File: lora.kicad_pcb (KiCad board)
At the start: 4 copper layers, 80.5 x 45 mm, 62 parts, among them J1 Conn_01x02, J11 Conn_Coaxial, J2 Humidity, J3 Temp, J4 Programming_Jumper, J5 Temp, J6 VDD, J7 GPS, J8 SIM800, J9 I2C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

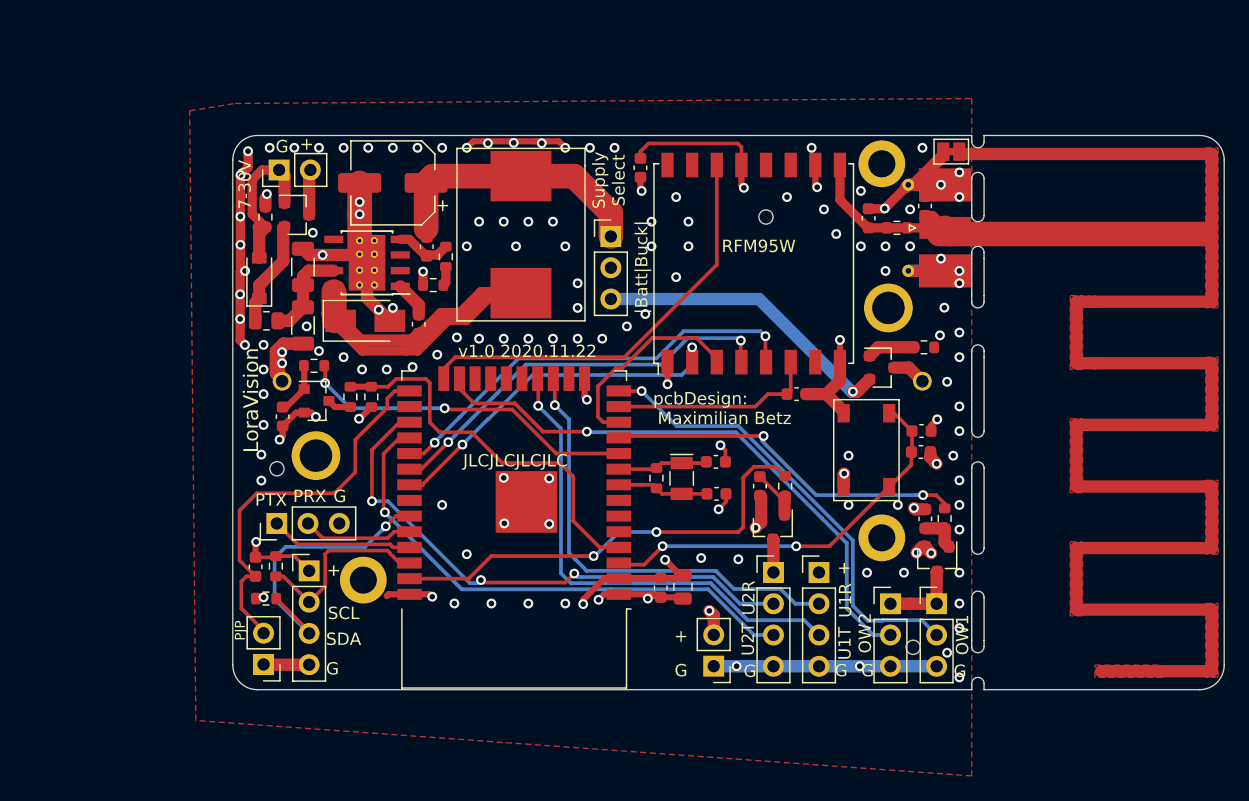
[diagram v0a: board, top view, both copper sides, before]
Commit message: updated pcb from schematic.
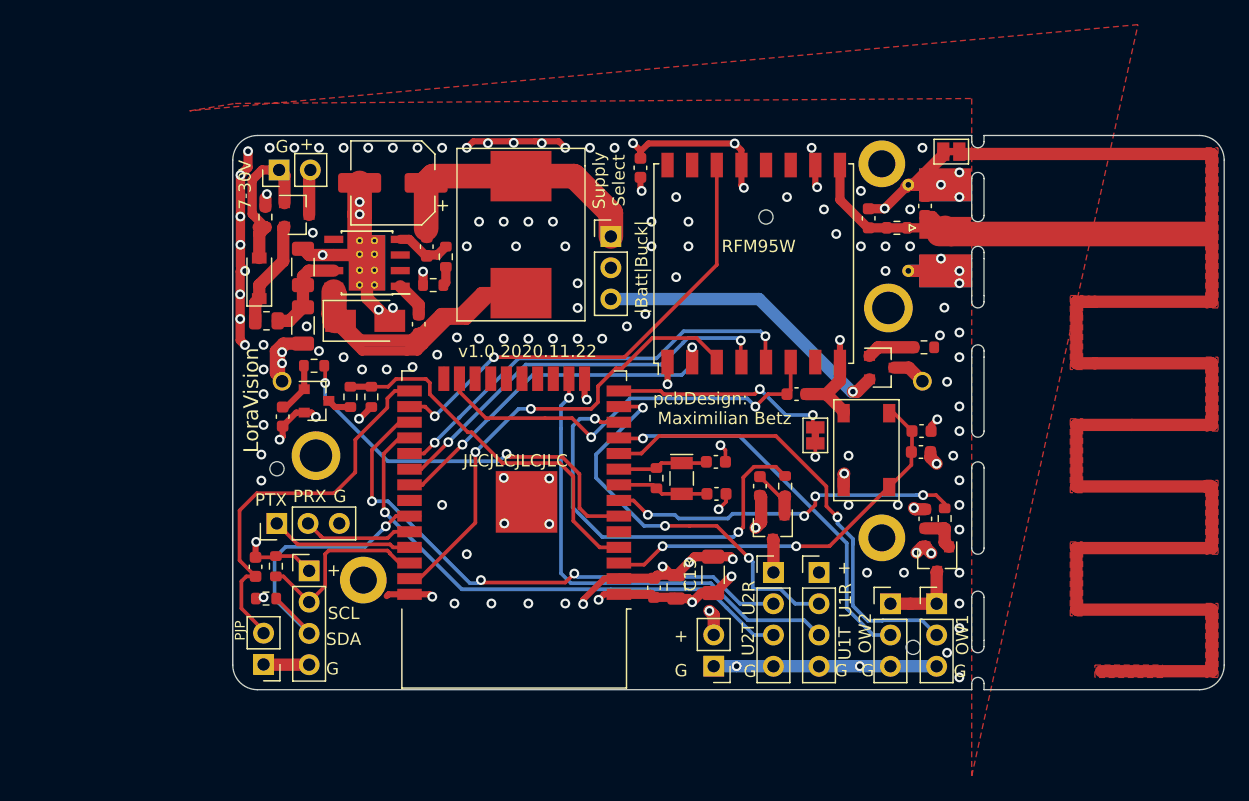
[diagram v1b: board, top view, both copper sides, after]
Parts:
- added C13: 100u, Capacitor_SMD:C_1206_3216Metric, F.Cu at (209.0, 127.7)
- added JP2: Bridged, Jumper:SolderJumper-2_P1.3mm_Bridged_Pad1.0x1.5mm, F.Cu at (217.3, 116.3)
- L2: value dnp -> 0R
- R14: value 7.5M -> dnp
- moved C6 0.55 mm to (204.2, 128.7)
- moved C7 0.55 mm to (206.0, 128.7)
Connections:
- U2 pad 10: VDD_SENSE_MOSFET_SWITCH -> ONEWIRE1_DATA
- U2 pad 11: VDD_SENSOR_MOSFET_SWITCH -> ONEWIRE2_DATA
- U2 pad 12: SPI_MOSI -> GPS_MOSFET_SWITCH
- U2 pad 13: RFM_RST -> UART1_RX
- U2 pad 14: ONEWIRE1_DATA -> Net-(JP2-Pad1)
- U2 pad 16: Net-(U2-Pad16) -> UART1_TX
- U2 pad 17: UART1_RX -> Net-(U2-Pad17)
- U2 pad 18: UART1_TX -> Net-(U2-Pad18)
- U2 pad 23: ONEWIRE2_DATA -> RFM_RST
- U2 pad 24: RFM_DIO0 -> Net-(U2-Pad24)
- U2 pad 26: Net-(U2-Pad26) -> RFM_DIO0
- U2 pad 37: GPS_MOSFET_SWITCH -> SPI_MOSI
- U2 pad 6: Net-(U2-Pad6) -> VDD_SENSE_MOSFET_SWITCH
- U2 pad 7: Net-(U2-Pad7) -> VDD_SENSOR_MOSFET_SWITCH
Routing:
- net SPI_MOSI: track 16.6 -> 38.3 mm, vias 0 -> 2
- net Net-(JP2-Pad1): track 0.00 -> 18.0 mm, vias 0 -> 2
- net RFM_RST: track 16.8 -> 34.7 mm, vias 0 -> 2
- net ONEWIRE2_DATA: track 47.0 -> 32.4 mm
- net VDD: track 45.0 -> 51.2 mm, vias 13 -> 18
- net VDD_SENSE_MOSFET_SWITCH: track 27.7 -> 32.6 mm
- net GND: track 135.2 -> 139.1 mm, vias 136 -> 135
- net RFM_DIO0: track 34.6 -> 38.5 mm, vias 0 -> 2
- net UART1_RX: track 36.7 -> 32.9 mm, vias 1 -> 3
- net GPS_MOSFET_SWITCH: track 36.9 -> 34.0 mm
- net VDD_SENSE: track 31.7 -> 30.4 mm
- net ONEWIRE1_DATA: track 37.1 -> 38.2 mm
- net Net-(U2-Pad24): track 0.00 -> 0.81 mm
- net VDD_SENSOR_MOSFET_SWITCH: track 30.3 -> 29.7 mm, vias 2 -> 4
- net UART1_TX: track 39.6 -> 39.1 mm

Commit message: added page legend.
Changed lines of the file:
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@@
   )
   (page A4)
+  (title_block
+    (title "Lora Vision   (as Sensor or Gateway)")
+    (date 2020-12-08)
+    (rev v1.0)
+  )
   (layers
     (0 F.Cu signal)
@@
     (polygon
       (pts
-        (xy 230 89) (xy 230 144) (xy 243.5 83) (xy 166.5 90) (xy 170.2 89.4)
+        (xy 230 89) (xy 230 144) (xy 153.1 143.5) (xy 166.5 90) (xy 170.2 89.4)
       )
     )
